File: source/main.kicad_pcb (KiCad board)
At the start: 2 copper layers, 0 parts

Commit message: Add basics
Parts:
- added D1: LED, lcsc:LED-SMD_L0.65-W0.35-P0.41_XL-0201SURC, F.Cu at (72.3, 40.0)
- added D2: LED, lcsc:LED-SMD_L0.65-W0.35-P0.41_XL-0201SURC, F.Cu at (72.3, 44.5)
- added P1: USB_Type_C_Receptacle_16_pin, lcsc:USB-C-SMD_TYPE-C-6PIN-2MD-073, F.Cu at (64.5, 41.3)
- added R1: 5.1kΩ, lcsc:R0402, F.Cu at (60.6, 47.9)
- added R2: 5.1kΩ, lcsc:R0402, F.Cu at (60.6, 50.1)
- added R3: 100Ω, lcsc:R0402, F.Cu at (60.6, 52.2)
- added R4: 100Ω, lcsc:R0402, F.Cu at (60.6, 54.4)

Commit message: Add WIP layout
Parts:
- added D10: LED, lcsc:LED-SMD_L0.65-W0.35-P0.41_XL-0201SURC, F.Cu at (35.1, -5.11)
- added D11: LED, lcsc:LED-SMD_L0.65-W0.35-P0.41_XL-0201SURC, F.Cu at (35.1, -7.31)
- added D12: LED, lcsc:LED-SMD_L0.65-W0.35-P0.41_XL-0201SURC, F.Cu at (4.61, -0.23)
- added D13: LED, lcsc:LED-SMD_L0.65-W0.35-P0.41_XL-0201SURC, F.Cu at (45.1, -13.4)
- added D14: LED, lcsc:LED-SMD_L0.65-W0.35-P0.41_XL-0201SURC, F.Cu at (49.6, -0.23)
- added D15: LED, lcsc:LED-SMD_L0.65-W0.35-P0.41_XL-0201SURC, F.Cu at (49.6, -2.43)
- added D16: LED, lcsc:LED-SMD_L0.65-W0.35-P0.41_XL-0201SURC, F.Cu at (49.6, -4.63)
- added D17: LED, lcsc:LED-SMD_L0.65-W0.35-P0.41_XL-0201SURC, F.Cu at (49.6, -6.83)
- added D18: LED, lcsc:LED-SMD_L0.65-W0.35-P0.41_XL-0201SURC, F.Cu at (49.6, -9.03)
- added D19: LED, lcsc:LED-SMD_L0.65-W0.35-P0.41_XL-0201SURC, F.Cu at (49.6, -11.2)
- added D20: LED, lcsc:LED-SMD_L0.65-W0.35-P0.41_XL-0201SURC, F.Cu at (49.6, -13.4)
- added D21: LED, lcsc:LED-SMD_L0.65-W0.35-P0.41_XL-0201SURC, F.Cu at (54.1, -13.4)
- added D22: LED, lcsc:LED-SMD_L0.65-W0.35-P0.41_XL-0201SURC, F.Cu at (4.61, -2.43)
- added D23: LED, lcsc:LED-SMD_L0.65-W0.35-P0.41_XL-0201SURC, F.Cu at (4.61, -4.63)
- added D24: LED, lcsc:LED-SMD_L0.65-W0.35-P0.41_XL-0201SURC, F.Cu at (4.61, -6.83)
- added D25: LED, lcsc:LED-SMD_L0.65-W0.35-P0.41_XL-0201SURC, F.Cu at (4.61, -9.03)
- added D26: LED, lcsc:LED-SMD_L0.65-W0.35-P0.41_XL-0201SURC, F.Cu at (4.61, -11.2)
- added D27: LED, lcsc:LED-SMD_L0.65-W0.35-P0.41_XL-0201SURC, F.Cu at (4.61, -13.4)
- added D28: LED, lcsc:LED-SMD_L0.65-W0.35-P0.41_XL-0201SURC, F.Cu at (9.11, -13.4)
- added D29: LED, lcsc:LED-SMD_L0.65-W0.35-P0.41_XL-0201SURC, F.Cu at (16.4, -1.52)
- added D3: LED, lcsc:LED-SMD_L0.65-W0.35-P0.41_XL-0201SURC, F.Cu at (16.4, -5.92)
- added D4: LED, lcsc:LED-SMD_L0.65-W0.35-P0.41_XL-0201SURC, F.Cu at (16.4, -8.12)
- added D5: LED, lcsc:LED-SMD_L0.65-W0.35-P0.41_XL-0201SURC, F.Cu at (16.4, -10.3)
- added D6: LED, lcsc:LED-SMD_L0.65-W0.35-P0.41_XL-0201SURC, F.Cu at (16.4, -12.5)
- added D7: LED, lcsc:LED-SMD_L0.65-W0.35-P0.41_XL-0201SURC, F.Cu at (20.9, -1.52)
- added D8: LED, lcsc:LED-SMD_L0.65-W0.35-P0.41_XL-0201SURC, F.Cu at (20.9, -8.12)
- added D9: LED, lcsc:LED-SMD_L0.65-W0.35-P0.41_XL-0201SURC, F.Cu at (20.9, -12.5)
- added R10: 100Ω, lcsc:R0402, F.Cu at (35.1, -6.11)
- added R11: 100Ω, lcsc:R0402, F.Cu at (35.1, -8.31)
- added R12: 100Ω, lcsc:R0402, F.Cu at (4.61, -1.23)
- added R13: 100Ω, lcsc:R0402, F.Cu at (45.1, -14.4)
- added R14: 100Ω, lcsc:R0402, F.Cu at (49.6, -1.23)
- added R15: 100Ω, lcsc:R0402, F.Cu at (49.6, -3.43)
- added R16: 100Ω, lcsc:R0402, F.Cu at (49.6, -5.63)
- added R17: 100Ω, lcsc:R0402, F.Cu at (49.6, -7.83)
- added R18: 100Ω, lcsc:R0402, F.Cu at (49.6, -10.0)
- added R19: 100Ω, lcsc:R0402, F.Cu at (49.6, -12.2)
- added R20: 100Ω, lcsc:R0402, F.Cu at (49.6, -14.4)
- added R21: 100Ω, lcsc:R0402, F.Cu at (54.1, -14.4)
- added R22: 100Ω, lcsc:R0402, F.Cu at (4.61, -3.43)
- added R23: 100Ω, lcsc:R0402, F.Cu at (4.61, -5.63)
- added R24: 100Ω, lcsc:R0402, F.Cu at (4.61, -7.83)
- added R25: 100Ω, lcsc:R0402, F.Cu at (4.61, -10.0)
- added R26: 100Ω, lcsc:R0402, F.Cu at (4.61, -12.2)
- added R27: 100Ω, lcsc:R0402, F.Cu at (4.61, -14.4)
- added R28: 100Ω, lcsc:R0402, F.Cu at (9.11, -14.4)
- added R29: 100Ω, lcsc:R0402, F.Cu at (16.4, -2.52)
- added R30: 5.1kΩ, lcsc:R0402, F.Cu at (49.3, -84.3)
- added R31: 5.1kΩ, lcsc:R0402, F.Cu at (49.3, -88.0)
- added R5: 100Ω, lcsc:R0402, F.Cu at (16.4, -11.3)
- added R6: 100Ω, lcsc:R0402, F.Cu at (16.4, -13.5)
- added R7: 100Ω, lcsc:R0402, F.Cu at (20.9, -2.52)
- added R8: 100Ω, lcsc:R0402, F.Cu at (20.9, -9.12)
- added R9: 100Ω, lcsc:R0402, F.Cu at (20.9, -13.5)
- R1, R2: value 5.1kΩ -> 100Ω
- moved P1 127.3 mm to (54.0, -85.6), turned to 90 degrees
- moved D1 89.8 mm to (0.11, -13.4)
- moved R1 86.9 mm to (0.11, -14.4), turned to 180 degrees
- moved R4 77.4 mm to (16.4, -9.12), turned to 180 degrees
- moved R3 73.8 mm to (16.4, -6.92), turned to 180 degrees
- moved D2 73.8 mm to (16.4, -3.72)
- moved R2 70.4 mm to (16.4, -4.72), turned to 180 degrees
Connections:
- D1 pad 1: D1-1-R3-1 -> D1-1-R1-1
- D1 pad 2: vbus -> D1-2-D10-2-D11-2-D12-2-D13-2-D14-2-D15-2-D16-2-D17-2-D18-2-D19-2-D2-2-D20-2-D21-2-D22-2-D23-2-D24-2-D25-2-D26-2-D27-2-D28-2-D29-2-D3-2-D4-2-D5-2-D6-2-D7-2-D8-2-D9-2
- D2 pad 1: D2-1-R4-1 -> D2-1-R2-1
- D2 pad 2: vbus -> D1-2-D10-2-D11-2-D12-2-D13-2-D14-2-D15-2-D16-2-D17-2-D18-2-D19-2-D2-2-D20-2-D21-2-D22-2-D23-2-D24-2-D25-2-D26-2-D27-2-D28-2-D29-2-D3-2-D4-2-D5-2-D6-2-D7-2-D8-2-D9-2
- P1 pad 11: vbus -> P1-11-P1-2
- P1 pad 2: vbus -> P1-11-P1-2
- P1 pad 4: P1-4-R1-1 -> P1-4-R30-1
- P1 pad 9: P1-9-R2-1 -> P1-9-R31-1
- R1 pad 1: P1-4-R1-1 -> D1-1-R1-1
- R1 pad 2: gnd -> R1-2-R10-2-R11-2-R12-2-R13-2-R14-2-R15-2-R16-2-R17-2-R18-2-R19-2-R2-2-R20-2-R21-2-R22-2-R23-2-R24-2-R25-2-R26-2-R27-2-R28-2-R29-2-R3-2-R4-2-R5-2-R6-2-R7-2-R8-2-R9-2
- R2 pad 1: P1-9-R2-1 -> D2-1-R2-1
- R2 pad 2: gnd -> R1-2-R10-2-R11-2-R12-2-R13-2-R14-2-R15-2-R16-2-R17-2-R18-2-R19-2-R2-2-R20-2-R21-2-R22-2-R23-2-R24-2-R25-2-R26-2-R27-2-R28-2-R29-2-R3-2-R4-2-R5-2-R6-2-R7-2-R8-2-R9-2
- R3 pad 1: D1-1-R3-1 -> D3-1-R3-1
- R3 pad 2: gnd -> R1-2-R10-2-R11-2-R12-2-R13-2-R14-2-R15-2-R16-2-R17-2-R18-2-R19-2-R2-2-R20-2-R21-2-R22-2-R23-2-R24-2-R25-2-R26-2-R27-2-R28-2-R29-2-R3-2-R4-2-R5-2-R6-2-R7-2-R8-2-R9-2
- R4 pad 1: D2-1-R4-1 -> D4-1-R4-1
- R4 pad 2: gnd -> R1-2-R10-2-R11-2-R12-2-R13-2-R14-2-R15-2-R16-2-R17-2-R18-2-R19-2-R2-2-R20-2-R21-2-R22-2-R23-2-R24-2-R25-2-R26-2-R27-2-R28-2-R29-2-R3-2-R4-2-R5-2-R6-2-R7-2-R8-2-R9-2
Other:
- board outline added: 85.6 x 54 mm

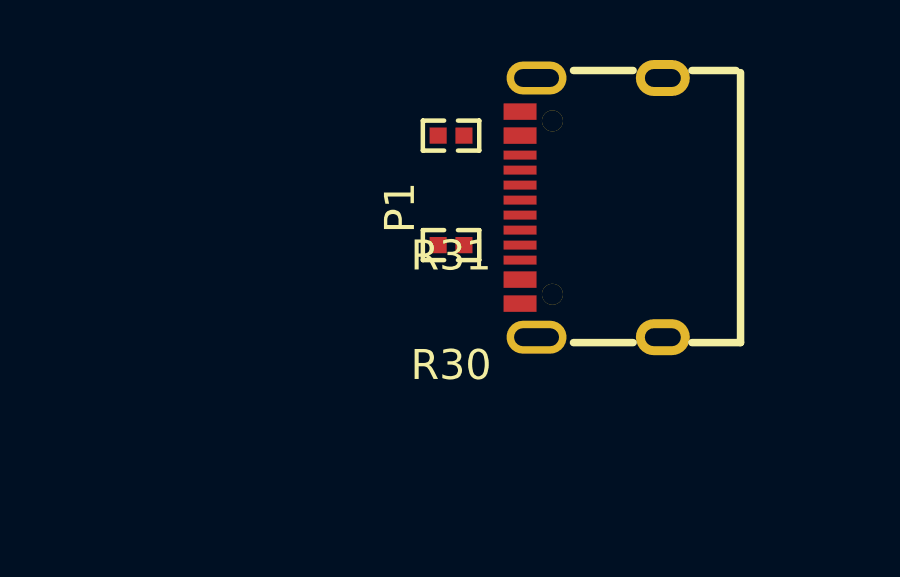
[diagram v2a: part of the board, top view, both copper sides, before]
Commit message: Better hierarchy layout; Fix pcb transform on no netlist change
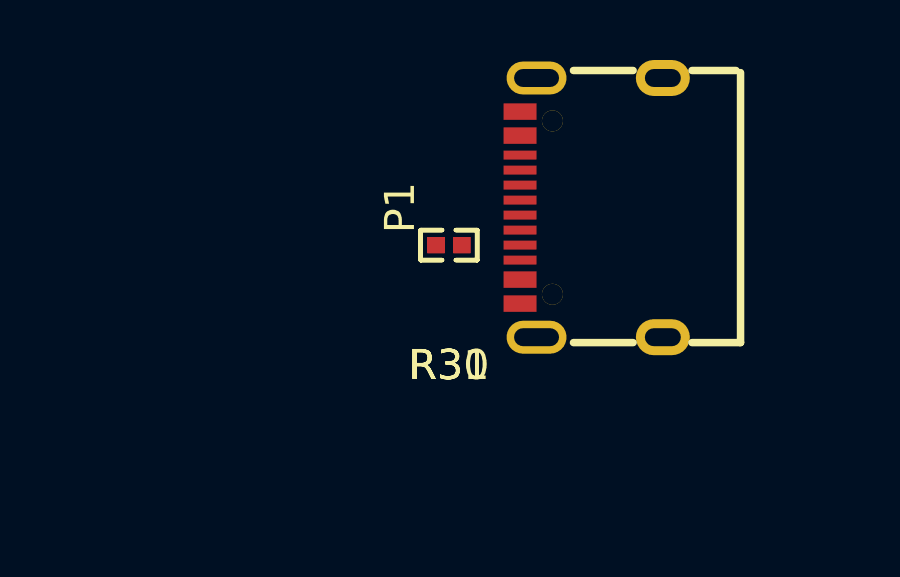
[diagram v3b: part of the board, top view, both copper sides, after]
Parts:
- moved R31 3.65 mm to (49.2, -84.3)
- moved R30 0.07 mm to (49.2, -84.3)
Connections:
- D1 pad 2: D1-2-D10-2-D11-2-D12-2-D13-2-D14-2-D15-2-D16-2-D17-2-D18-2-D19-2-D2-2-D20-2-D21-2-D22-2-D23-2-D24-2-D25-2-D26-2-D27-2-D28-2-D29-2-D3-2-D4-2-D5-2-D6-2-D7-2-D8-2-D9-2 -> D1-2
- D10 pad 2: D1-2-D10-2-D11-2-D12-2-D13-2-D14-2-D15-2-D16-2-D17-2-D18-2-D19-2-D2-2-D20-2-D21-2-D22-2-D23-2-D24-2-D25-2-D26-2-D27-2-D28-2-D29-2-D3-2-D4-2-D5-2-D6-2-D7-2-D8-2-D9-2 -> D10-2
- D11 pad 2: D1-2-D10-2-D11-2-D12-2-D13-2-D14-2-D15-2-D16-2-D17-2-D18-2-D19-2-D2-2-D20-2-D21-2-D22-2-D23-2-D24-2-D25-2-D26-2-D27-2-D28-2-D29-2-D3-2-D4-2-D5-2-D6-2-D7-2-D8-2-D9-2 -> D11-2
- D12 pad 2: D1-2-D10-2-D11-2-D12-2-D13-2-D14-2-D15-2-D16-2-D17-2-D18-2-D19-2-D2-2-D20-2-D21-2-D22-2-D23-2-D24-2-D25-2-D26-2-D27-2-D28-2-D29-2-D3-2-D4-2-D5-2-D6-2-D7-2-D8-2-D9-2 -> D12-2
- D13 pad 2: D1-2-D10-2-D11-2-D12-2-D13-2-D14-2-D15-2-D16-2-D17-2-D18-2-D19-2-D2-2-D20-2-D21-2-D22-2-D23-2-D24-2-D25-2-D26-2-D27-2-D28-2-D29-2-D3-2-D4-2-D5-2-D6-2-D7-2-D8-2-D9-2 -> D13-2
- D14 pad 2: D1-2-D10-2-D11-2-D12-2-D13-2-D14-2-D15-2-D16-2-D17-2-D18-2-D19-2-D2-2-D20-2-D21-2-D22-2-D23-2-D24-2-D25-2-D26-2-D27-2-D28-2-D29-2-D3-2-D4-2-D5-2-D6-2-D7-2-D8-2-D9-2 -> D14-2
- D15 pad 2: D1-2-D10-2-D11-2-D12-2-D13-2-D14-2-D15-2-D16-2-D17-2-D18-2-D19-2-D2-2-D20-2-D21-2-D22-2-D23-2-D24-2-D25-2-D26-2-D27-2-D28-2-D29-2-D3-2-D4-2-D5-2-D6-2-D7-2-D8-2-D9-2 -> D15-2
- D16 pad 2: D1-2-D10-2-D11-2-D12-2-D13-2-D14-2-D15-2-D16-2-D17-2-D18-2-D19-2-D2-2-D20-2-D21-2-D22-2-D23-2-D24-2-D25-2-D26-2-D27-2-D28-2-D29-2-D3-2-D4-2-D5-2-D6-2-D7-2-D8-2-D9-2 -> D16-2
- D17 pad 2: D1-2-D10-2-D11-2-D12-2-D13-2-D14-2-D15-2-D16-2-D17-2-D18-2-D19-2-D2-2-D20-2-D21-2-D22-2-D23-2-D24-2-D25-2-D26-2-D27-2-D28-2-D29-2-D3-2-D4-2-D5-2-D6-2-D7-2-D8-2-D9-2 -> D17-2
- D18 pad 2: D1-2-D10-2-D11-2-D12-2-D13-2-D14-2-D15-2-D16-2-D17-2-D18-2-D19-2-D2-2-D20-2-D21-2-D22-2-D23-2-D24-2-D25-2-D26-2-D27-2-D28-2-D29-2-D3-2-D4-2-D5-2-D6-2-D7-2-D8-2-D9-2 -> D18-2
- D19 pad 2: D1-2-D10-2-D11-2-D12-2-D13-2-D14-2-D15-2-D16-2-D17-2-D18-2-D19-2-D2-2-D20-2-D21-2-D22-2-D23-2-D24-2-D25-2-D26-2-D27-2-D28-2-D29-2-D3-2-D4-2-D5-2-D6-2-D7-2-D8-2-D9-2 -> D19-2
- D2 pad 2: D1-2-D10-2-D11-2-D12-2-D13-2-D14-2-D15-2-D16-2-D17-2-D18-2-D19-2-D2-2-D20-2-D21-2-D22-2-D23-2-D24-2-D25-2-D26-2-D27-2-D28-2-D29-2-D3-2-D4-2-D5-2-D6-2-D7-2-D8-2-D9-2 -> D2-2
- D20 pad 2: D1-2-D10-2-D11-2-D12-2-D13-2-D14-2-D15-2-D16-2-D17-2-D18-2-D19-2-D2-2-D20-2-D21-2-D22-2-D23-2-D24-2-D25-2-D26-2-D27-2-D28-2-D29-2-D3-2-D4-2-D5-2-D6-2-D7-2-D8-2-D9-2 -> D20-2
- D21 pad 2: D1-2-D10-2-D11-2-D12-2-D13-2-D14-2-D15-2-D16-2-D17-2-D18-2-D19-2-D2-2-D20-2-D21-2-D22-2-D23-2-D24-2-D25-2-D26-2-D27-2-D28-2-D29-2-D3-2-D4-2-D5-2-D6-2-D7-2-D8-2-D9-2 -> D21-2
- D22 pad 2: D1-2-D10-2-D11-2-D12-2-D13-2-D14-2-D15-2-D16-2-D17-2-D18-2-D19-2-D2-2-D20-2-D21-2-D22-2-D23-2-D24-2-D25-2-D26-2-D27-2-D28-2-D29-2-D3-2-D4-2-D5-2-D6-2-D7-2-D8-2-D9-2 -> D22-2
- D23 pad 2: D1-2-D10-2-D11-2-D12-2-D13-2-D14-2-D15-2-D16-2-D17-2-D18-2-D19-2-D2-2-D20-2-D21-2-D22-2-D23-2-D24-2-D25-2-D26-2-D27-2-D28-2-D29-2-D3-2-D4-2-D5-2-D6-2-D7-2-D8-2-D9-2 -> D23-2
- D24 pad 2: D1-2-D10-2-D11-2-D12-2-D13-2-D14-2-D15-2-D16-2-D17-2-D18-2-D19-2-D2-2-D20-2-D21-2-D22-2-D23-2-D24-2-D25-2-D26-2-D27-2-D28-2-D29-2-D3-2-D4-2-D5-2-D6-2-D7-2-D8-2-D9-2 -> D24-2
- D25 pad 2: D1-2-D10-2-D11-2-D12-2-D13-2-D14-2-D15-2-D16-2-D17-2-D18-2-D19-2-D2-2-D20-2-D21-2-D22-2-D23-2-D24-2-D25-2-D26-2-D27-2-D28-2-D29-2-D3-2-D4-2-D5-2-D6-2-D7-2-D8-2-D9-2 -> D25-2
- D26 pad 2: D1-2-D10-2-D11-2-D12-2-D13-2-D14-2-D15-2-D16-2-D17-2-D18-2-D19-2-D2-2-D20-2-D21-2-D22-2-D23-2-D24-2-D25-2-D26-2-D27-2-D28-2-D29-2-D3-2-D4-2-D5-2-D6-2-D7-2-D8-2-D9-2 -> D26-2
- D27 pad 2: D1-2-D10-2-D11-2-D12-2-D13-2-D14-2-D15-2-D16-2-D17-2-D18-2-D19-2-D2-2-D20-2-D21-2-D22-2-D23-2-D24-2-D25-2-D26-2-D27-2-D28-2-D29-2-D3-2-D4-2-D5-2-D6-2-D7-2-D8-2-D9-2 -> D27-2
- D28 pad 2: D1-2-D10-2-D11-2-D12-2-D13-2-D14-2-D15-2-D16-2-D17-2-D18-2-D19-2-D2-2-D20-2-D21-2-D22-2-D23-2-D24-2-D25-2-D26-2-D27-2-D28-2-D29-2-D3-2-D4-2-D5-2-D6-2-D7-2-D8-2-D9-2 -> D28-2
- D29 pad 2: D1-2-D10-2-D11-2-D12-2-D13-2-D14-2-D15-2-D16-2-D17-2-D18-2-D19-2-D2-2-D20-2-D21-2-D22-2-D23-2-D24-2-D25-2-D26-2-D27-2-D28-2-D29-2-D3-2-D4-2-D5-2-D6-2-D7-2-D8-2-D9-2 -> D29-2
- D3 pad 2: D1-2-D10-2-D11-2-D12-2-D13-2-D14-2-D15-2-D16-2-D17-2-D18-2-D19-2-D2-2-D20-2-D21-2-D22-2-D23-2-D24-2-D25-2-D26-2-D27-2-D28-2-D29-2-D3-2-D4-2-D5-2-D6-2-D7-2-D8-2-D9-2 -> D3-2
- D4 pad 2: D1-2-D10-2-D11-2-D12-2-D13-2-D14-2-D15-2-D16-2-D17-2-D18-2-D19-2-D2-2-D20-2-D21-2-D22-2-D23-2-D24-2-D25-2-D26-2-D27-2-D28-2-D29-2-D3-2-D4-2-D5-2-D6-2-D7-2-D8-2-D9-2 -> D4-2
- D5 pad 2: D1-2-D10-2-D11-2-D12-2-D13-2-D14-2-D15-2-D16-2-D17-2-D18-2-D19-2-D2-2-D20-2-D21-2-D22-2-D23-2-D24-2-D25-2-D26-2-D27-2-D28-2-D29-2-D3-2-D4-2-D5-2-D6-2-D7-2-D8-2-D9-2 -> D5-2
- D6 pad 2: D1-2-D10-2-D11-2-D12-2-D13-2-D14-2-D15-2-D16-2-D17-2-D18-2-D19-2-D2-2-D20-2-D21-2-D22-2-D23-2-D24-2-D25-2-D26-2-D27-2-D28-2-D29-2-D3-2-D4-2-D5-2-D6-2-D7-2-D8-2-D9-2 -> D6-2
- D7 pad 2: D1-2-D10-2-D11-2-D12-2-D13-2-D14-2-D15-2-D16-2-D17-2-D18-2-D19-2-D2-2-D20-2-D21-2-D22-2-D23-2-D24-2-D25-2-D26-2-D27-2-D28-2-D29-2-D3-2-D4-2-D5-2-D6-2-D7-2-D8-2-D9-2 -> D7-2
- D8 pad 2: D1-2-D10-2-D11-2-D12-2-D13-2-D14-2-D15-2-D16-2-D17-2-D18-2-D19-2-D2-2-D20-2-D21-2-D22-2-D23-2-D24-2-D25-2-D26-2-D27-2-D28-2-D29-2-D3-2-D4-2-D5-2-D6-2-D7-2-D8-2-D9-2 -> D8-2
- D9 pad 2: D1-2-D10-2-D11-2-D12-2-D13-2-D14-2-D15-2-D16-2-D17-2-D18-2-D19-2-D2-2-D20-2-D21-2-D22-2-D23-2-D24-2-D25-2-D26-2-D27-2-D28-2-D29-2-D3-2-D4-2-D5-2-D6-2-D7-2-D8-2-D9-2 -> D9-2
- R1 pad 2: R1-2-R10-2-R11-2-R12-2-R13-2-R14-2-R15-2-R16-2-R17-2-R18-2-R19-2-R2-2-R20-2-R21-2-R22-2-R23-2-R24-2-R25-2-R26-2-R27-2-R28-2-R29-2-R3-2-R4-2-R5-2-R6-2-R7-2-R8-2-R9-2 -> R1-2
- R10 pad 2: R1-2-R10-2-R11-2-R12-2-R13-2-R14-2-R15-2-R16-2-R17-2-R18-2-R19-2-R2-2-R20-2-R21-2-R22-2-R23-2-R24-2-R25-2-R26-2-R27-2-R28-2-R29-2-R3-2-R4-2-R5-2-R6-2-R7-2-R8-2-R9-2 -> R10-2
- R11 pad 2: R1-2-R10-2-R11-2-R12-2-R13-2-R14-2-R15-2-R16-2-R17-2-R18-2-R19-2-R2-2-R20-2-R21-2-R22-2-R23-2-R24-2-R25-2-R26-2-R27-2-R28-2-R29-2-R3-2-R4-2-R5-2-R6-2-R7-2-R8-2-R9-2 -> R11-2
- R12 pad 2: R1-2-R10-2-R11-2-R12-2-R13-2-R14-2-R15-2-R16-2-R17-2-R18-2-R19-2-R2-2-R20-2-R21-2-R22-2-R23-2-R24-2-R25-2-R26-2-R27-2-R28-2-R29-2-R3-2-R4-2-R5-2-R6-2-R7-2-R8-2-R9-2 -> R12-2
- R13 pad 2: R1-2-R10-2-R11-2-R12-2-R13-2-R14-2-R15-2-R16-2-R17-2-R18-2-R19-2-R2-2-R20-2-R21-2-R22-2-R23-2-R24-2-R25-2-R26-2-R27-2-R28-2-R29-2-R3-2-R4-2-R5-2-R6-2-R7-2-R8-2-R9-2 -> R13-2
- R14 pad 2: R1-2-R10-2-R11-2-R12-2-R13-2-R14-2-R15-2-R16-2-R17-2-R18-2-R19-2-R2-2-R20-2-R21-2-R22-2-R23-2-R24-2-R25-2-R26-2-R27-2-R28-2-R29-2-R3-2-R4-2-R5-2-R6-2-R7-2-R8-2-R9-2 -> R14-2
- R15 pad 2: R1-2-R10-2-R11-2-R12-2-R13-2-R14-2-R15-2-R16-2-R17-2-R18-2-R19-2-R2-2-R20-2-R21-2-R22-2-R23-2-R24-2-R25-2-R26-2-R27-2-R28-2-R29-2-R3-2-R4-2-R5-2-R6-2-R7-2-R8-2-R9-2 -> R15-2
- R16 pad 2: R1-2-R10-2-R11-2-R12-2-R13-2-R14-2-R15-2-R16-2-R17-2-R18-2-R19-2-R2-2-R20-2-R21-2-R22-2-R23-2-R24-2-R25-2-R26-2-R27-2-R28-2-R29-2-R3-2-R4-2-R5-2-R6-2-R7-2-R8-2-R9-2 -> R16-2
- R17 pad 2: R1-2-R10-2-R11-2-R12-2-R13-2-R14-2-R15-2-R16-2-R17-2-R18-2-R19-2-R2-2-R20-2-R21-2-R22-2-R23-2-R24-2-R25-2-R26-2-R27-2-R28-2-R29-2-R3-2-R4-2-R5-2-R6-2-R7-2-R8-2-R9-2 -> R17-2
- R18 pad 2: R1-2-R10-2-R11-2-R12-2-R13-2-R14-2-R15-2-R16-2-R17-2-R18-2-R19-2-R2-2-R20-2-R21-2-R22-2-R23-2-R24-2-R25-2-R26-2-R27-2-R28-2-R29-2-R3-2-R4-2-R5-2-R6-2-R7-2-R8-2-R9-2 -> R18-2
- R19 pad 2: R1-2-R10-2-R11-2-R12-2-R13-2-R14-2-R15-2-R16-2-R17-2-R18-2-R19-2-R2-2-R20-2-R21-2-R22-2-R23-2-R24-2-R25-2-R26-2-R27-2-R28-2-R29-2-R3-2-R4-2-R5-2-R6-2-R7-2-R8-2-R9-2 -> R19-2
- R2 pad 2: R1-2-R10-2-R11-2-R12-2-R13-2-R14-2-R15-2-R16-2-R17-2-R18-2-R19-2-R2-2-R20-2-R21-2-R22-2-R23-2-R24-2-R25-2-R26-2-R27-2-R28-2-R29-2-R3-2-R4-2-R5-2-R6-2-R7-2-R8-2-R9-2 -> R2-2
- R20 pad 2: R1-2-R10-2-R11-2-R12-2-R13-2-R14-2-R15-2-R16-2-R17-2-R18-2-R19-2-R2-2-R20-2-R21-2-R22-2-R23-2-R24-2-R25-2-R26-2-R27-2-R28-2-R29-2-R3-2-R4-2-R5-2-R6-2-R7-2-R8-2-R9-2 -> R20-2
- R21 pad 2: R1-2-R10-2-R11-2-R12-2-R13-2-R14-2-R15-2-R16-2-R17-2-R18-2-R19-2-R2-2-R20-2-R21-2-R22-2-R23-2-R24-2-R25-2-R26-2-R27-2-R28-2-R29-2-R3-2-R4-2-R5-2-R6-2-R7-2-R8-2-R9-2 -> R21-2
- R22 pad 2: R1-2-R10-2-R11-2-R12-2-R13-2-R14-2-R15-2-R16-2-R17-2-R18-2-R19-2-R2-2-R20-2-R21-2-R22-2-R23-2-R24-2-R25-2-R26-2-R27-2-R28-2-R29-2-R3-2-R4-2-R5-2-R6-2-R7-2-R8-2-R9-2 -> R22-2
- R23 pad 2: R1-2-R10-2-R11-2-R12-2-R13-2-R14-2-R15-2-R16-2-R17-2-R18-2-R19-2-R2-2-R20-2-R21-2-R22-2-R23-2-R24-2-R25-2-R26-2-R27-2-R28-2-R29-2-R3-2-R4-2-R5-2-R6-2-R7-2-R8-2-R9-2 -> R23-2
- R24 pad 2: R1-2-R10-2-R11-2-R12-2-R13-2-R14-2-R15-2-R16-2-R17-2-R18-2-R19-2-R2-2-R20-2-R21-2-R22-2-R23-2-R24-2-R25-2-R26-2-R27-2-R28-2-R29-2-R3-2-R4-2-R5-2-R6-2-R7-2-R8-2-R9-2 -> R24-2
- R25 pad 2: R1-2-R10-2-R11-2-R12-2-R13-2-R14-2-R15-2-R16-2-R17-2-R18-2-R19-2-R2-2-R20-2-R21-2-R22-2-R23-2-R24-2-R25-2-R26-2-R27-2-R28-2-R29-2-R3-2-R4-2-R5-2-R6-2-R7-2-R8-2-R9-2 -> R25-2
- R26 pad 2: R1-2-R10-2-R11-2-R12-2-R13-2-R14-2-R15-2-R16-2-R17-2-R18-2-R19-2-R2-2-R20-2-R21-2-R22-2-R23-2-R24-2-R25-2-R26-2-R27-2-R28-2-R29-2-R3-2-R4-2-R5-2-R6-2-R7-2-R8-2-R9-2 -> R26-2
- R27 pad 2: R1-2-R10-2-R11-2-R12-2-R13-2-R14-2-R15-2-R16-2-R17-2-R18-2-R19-2-R2-2-R20-2-R21-2-R22-2-R23-2-R24-2-R25-2-R26-2-R27-2-R28-2-R29-2-R3-2-R4-2-R5-2-R6-2-R7-2-R8-2-R9-2 -> R27-2
- R28 pad 2: R1-2-R10-2-R11-2-R12-2-R13-2-R14-2-R15-2-R16-2-R17-2-R18-2-R19-2-R2-2-R20-2-R21-2-R22-2-R23-2-R24-2-R25-2-R26-2-R27-2-R28-2-R29-2-R3-2-R4-2-R5-2-R6-2-R7-2-R8-2-R9-2 -> R28-2
- R29 pad 2: R1-2-R10-2-R11-2-R12-2-R13-2-R14-2-R15-2-R16-2-R17-2-R18-2-R19-2-R2-2-R20-2-R21-2-R22-2-R23-2-R24-2-R25-2-R26-2-R27-2-R28-2-R29-2-R3-2-R4-2-R5-2-R6-2-R7-2-R8-2-R9-2 -> R29-2
- R3 pad 2: R1-2-R10-2-R11-2-R12-2-R13-2-R14-2-R15-2-R16-2-R17-2-R18-2-R19-2-R2-2-R20-2-R21-2-R22-2-R23-2-R24-2-R25-2-R26-2-R27-2-R28-2-R29-2-R3-2-R4-2-R5-2-R6-2-R7-2-R8-2-R9-2 -> R3-2
- R4 pad 2: R1-2-R10-2-R11-2-R12-2-R13-2-R14-2-R15-2-R16-2-R17-2-R18-2-R19-2-R2-2-R20-2-R21-2-R22-2-R23-2-R24-2-R25-2-R26-2-R27-2-R28-2-R29-2-R3-2-R4-2-R5-2-R6-2-R7-2-R8-2-R9-2 -> R4-2
- R5 pad 2: R1-2-R10-2-R11-2-R12-2-R13-2-R14-2-R15-2-R16-2-R17-2-R18-2-R19-2-R2-2-R20-2-R21-2-R22-2-R23-2-R24-2-R25-2-R26-2-R27-2-R28-2-R29-2-R3-2-R4-2-R5-2-R6-2-R7-2-R8-2-R9-2 -> R5-2
- R6 pad 2: R1-2-R10-2-R11-2-R12-2-R13-2-R14-2-R15-2-R16-2-R17-2-R18-2-R19-2-R2-2-R20-2-R21-2-R22-2-R23-2-R24-2-R25-2-R26-2-R27-2-R28-2-R29-2-R3-2-R4-2-R5-2-R6-2-R7-2-R8-2-R9-2 -> R6-2
- R7 pad 2: R1-2-R10-2-R11-2-R12-2-R13-2-R14-2-R15-2-R16-2-R17-2-R18-2-R19-2-R2-2-R20-2-R21-2-R22-2-R23-2-R24-2-R25-2-R26-2-R27-2-R28-2-R29-2-R3-2-R4-2-R5-2-R6-2-R7-2-R8-2-R9-2 -> R7-2
- R8 pad 2: R1-2-R10-2-R11-2-R12-2-R13-2-R14-2-R15-2-R16-2-R17-2-R18-2-R19-2-R2-2-R20-2-R21-2-R22-2-R23-2-R24-2-R25-2-R26-2-R27-2-R28-2-R29-2-R3-2-R4-2-R5-2-R6-2-R7-2-R8-2-R9-2 -> R8-2
- R9 pad 2: R1-2-R10-2-R11-2-R12-2-R13-2-R14-2-R15-2-R16-2-R17-2-R18-2-R19-2-R2-2-R20-2-R21-2-R22-2-R23-2-R24-2-R25-2-R26-2-R27-2-R28-2-R29-2-R3-2-R4-2-R5-2-R6-2-R7-2-R8-2-R9-2 -> R9-2

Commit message: Fix layout
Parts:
- moved R30 147.9 mm to (86.8, 58.7)
- moved R31 147.9 mm to (86.8, 58.7)
- moved P1 143.1 mm to (85.6, 54.0)
- moved R19 2.00 mm to (49.6, -10.2)
- moved R26 2.00 mm to (4.61, -10.2)
- moved R12 2.00 mm to (4.61, 0.77)
- moved R14 2.00 mm to (49.6, 0.77)
- moved R15 2.00 mm to (49.6, -1.43)
- moved R22 2.00 mm to (4.61, -1.43)
- moved R1 2.00 mm to (0.11, -12.4)
- moved R13 2.00 mm to (45.1, -12.4)
- moved R16 2.00 mm to (49.6, -3.63)
- moved R17 2.00 mm to (49.6, -5.83)
- moved R18 2.00 mm to (49.6, -8.03)
- moved R20 2.00 mm to (49.6, -12.4)
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
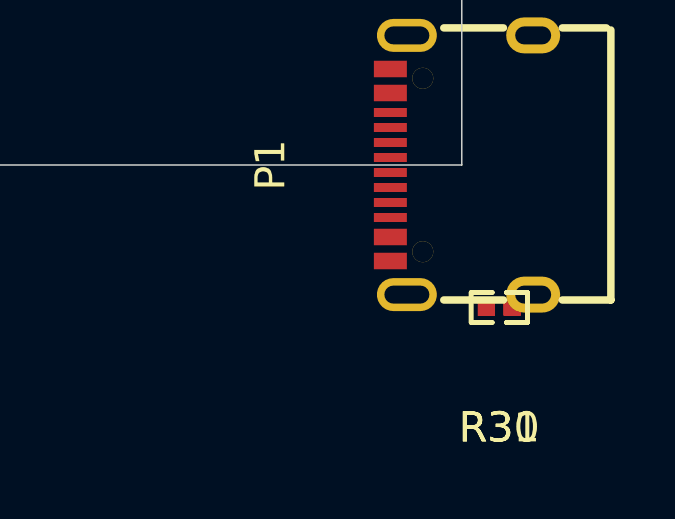
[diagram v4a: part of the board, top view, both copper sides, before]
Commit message: Use new hierarchical layout
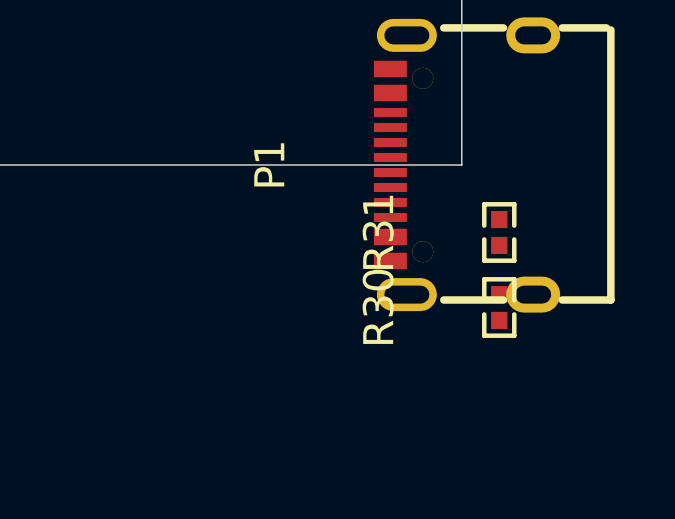
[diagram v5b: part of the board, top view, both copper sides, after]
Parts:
- moved R31 2.50 mm to (86.8, 56.2), turned to 90 degrees
- turned R30 to 90 degrees

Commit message: wip:
- add outline with rounded corners
- add logo
- add more layout
- insert vias for vbus anode led
- move designators
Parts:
- removed D21: LED, lcsc:LED-SMD_L0.65-W0.35-P0.41_XL-0201SURC
- removed R21: 100Ω, lcsc:R0402
- added C1: 100nF 16V X7R, lcsc:C0402, F.Cu at (74.1, 27.0)
- added F1: Fuse, lcsc:F0402, F.Cu at (76.3, 29.5)
- added LOGO1: Faebryk_Logo, logo:faebryk_logo, F.Cu at (42.8, 41.0)
- D1, D10, D11, D12, D13, D14, D15, D16, D17, D18, D19, D2, D20, D22, D23, D24, D25, D26, D27, D28, D29, D3, D4, D5, D6, D7, D8, D9: footprint lcsc:LED-SMD_L0.65-W0.35-P0.41_XL-0201SURC -> lcsc:LED0402-R-RD_RED
- moved D27 57.8 mm to (37.9, 33.8)
- moved R27 57.8 mm to (37.9, 34.8)
- moved D28 52.8 mm to (37.9, 30.8)
- moved R28 52.8 mm to (37.9, 31.8)
- moved D4 49.1 mm to (41.9, 33.8)
- moved R4 49.1 mm to (41.9, 34.8)
- moved D7 47.7 mm to (52.9, 33.8)
- moved R7 47.7 mm to (52.9, 34.8)
- moved D9 47.0 mm to (52.9, 21.8)
- moved R9 47.0 mm to (52.9, 22.8)
- moved D8 45.9 mm to (52.9, 24.8)
- moved R8 45.9 mm to (52.9, 25.8)
- moved D10 44.6 mm to (56.9, 33.8)
- moved R10 44.6 mm to (56.9, 34.8)
- moved D20 44.0 mm to (75.9, 21.8)
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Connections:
- net P1-11-P1-2 renamed F1-1-P1-11-P1-2
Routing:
- net D9-2: vias 0 -> 1
- net D8-2: vias 0 -> 1
- net D7-2: vias 0 -> 1
- net D6-2: vias 0 -> 1
- net D5-2: vias 0 -> 1
- net D4-2: vias 0 -> 1
- net D3-2: vias 0 -> 1
- net D29-2: vias 0 -> 1
- net D28-2: vias 0 -> 1
- net D27-2: vias 0 -> 1
- net D26-2: vias 0 -> 1
- net D25-2: vias 0 -> 1
- net D24-2: vias 0 -> 1
- net D23-2: vias 0 -> 1
- net D22-2: vias 0 -> 1
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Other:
- board size 85.6 x 54 mm -> 88.6 x 60 mm

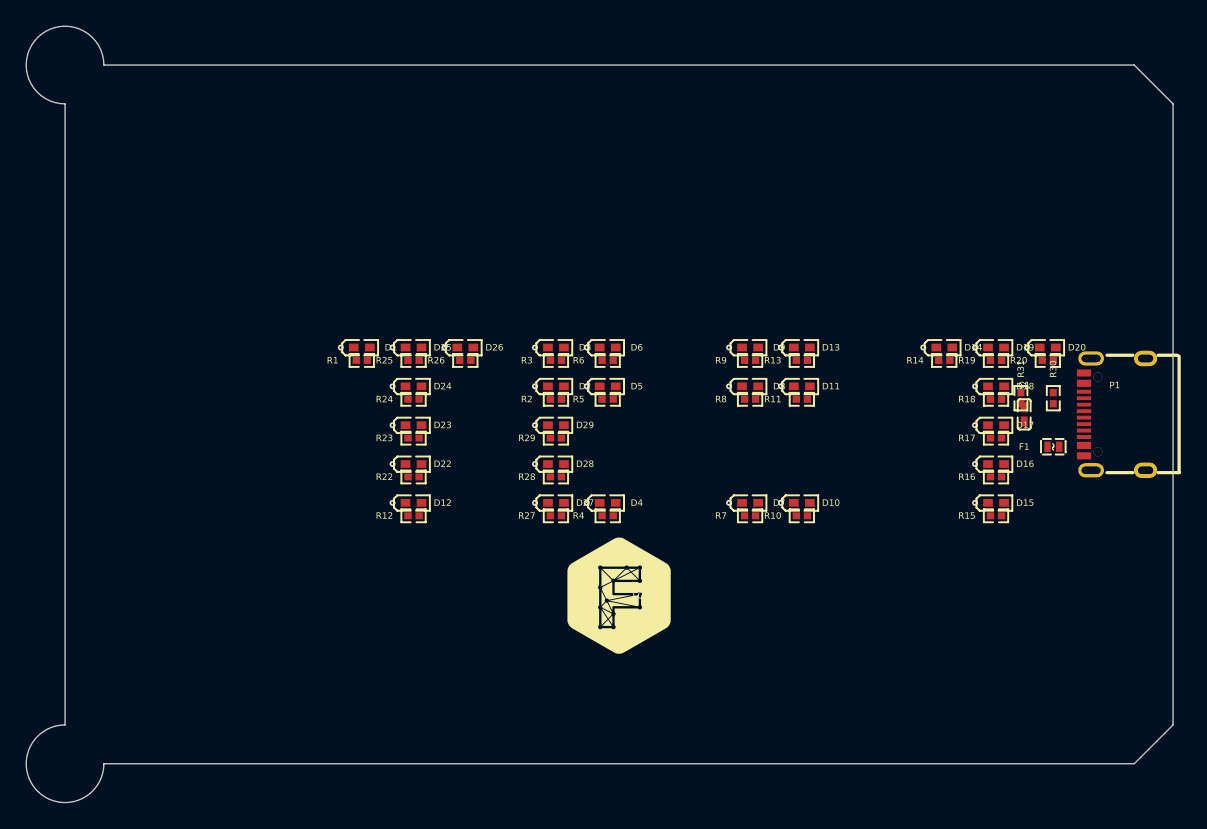
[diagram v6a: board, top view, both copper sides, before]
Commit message: Rename edgecut function; Set correct creditcard corner radius
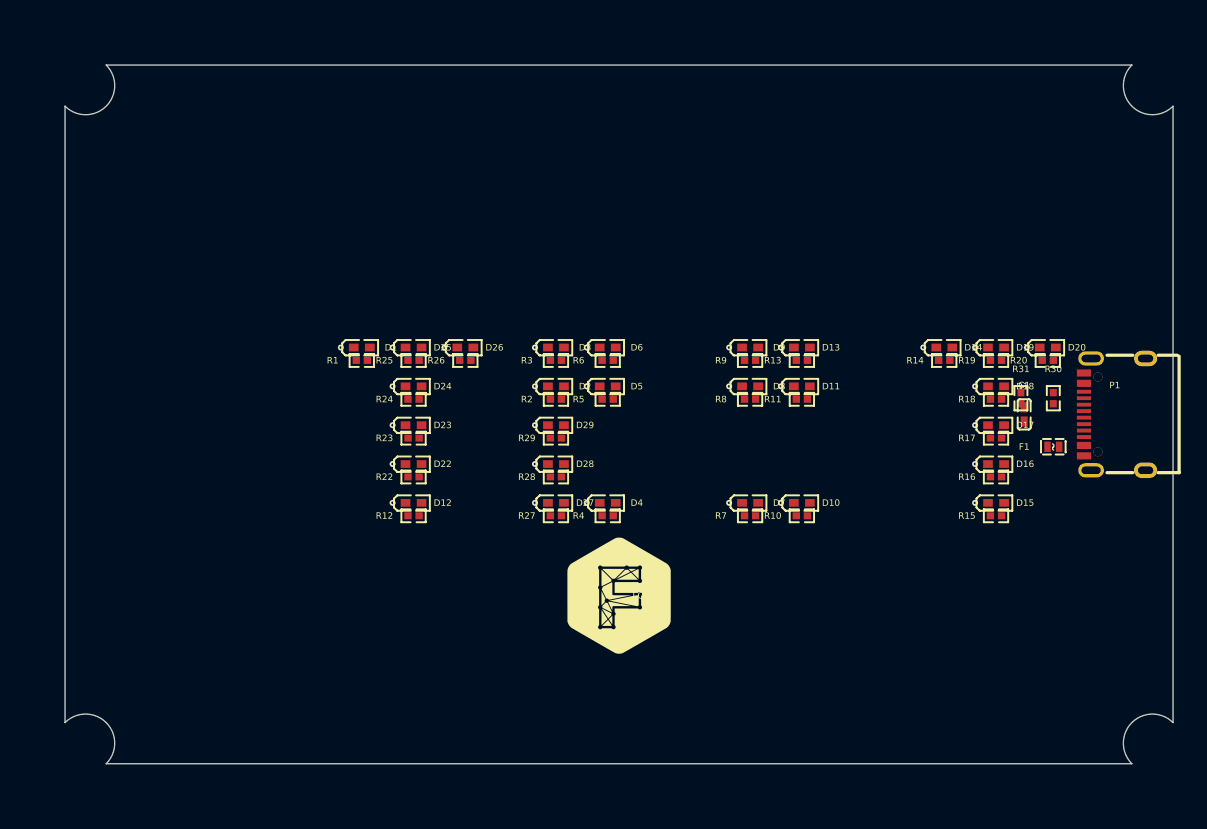
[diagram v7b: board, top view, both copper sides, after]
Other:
- board size 88.6 x 60 mm -> 85.6 x 54 mm
